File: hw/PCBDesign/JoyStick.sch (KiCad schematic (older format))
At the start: 4 parts

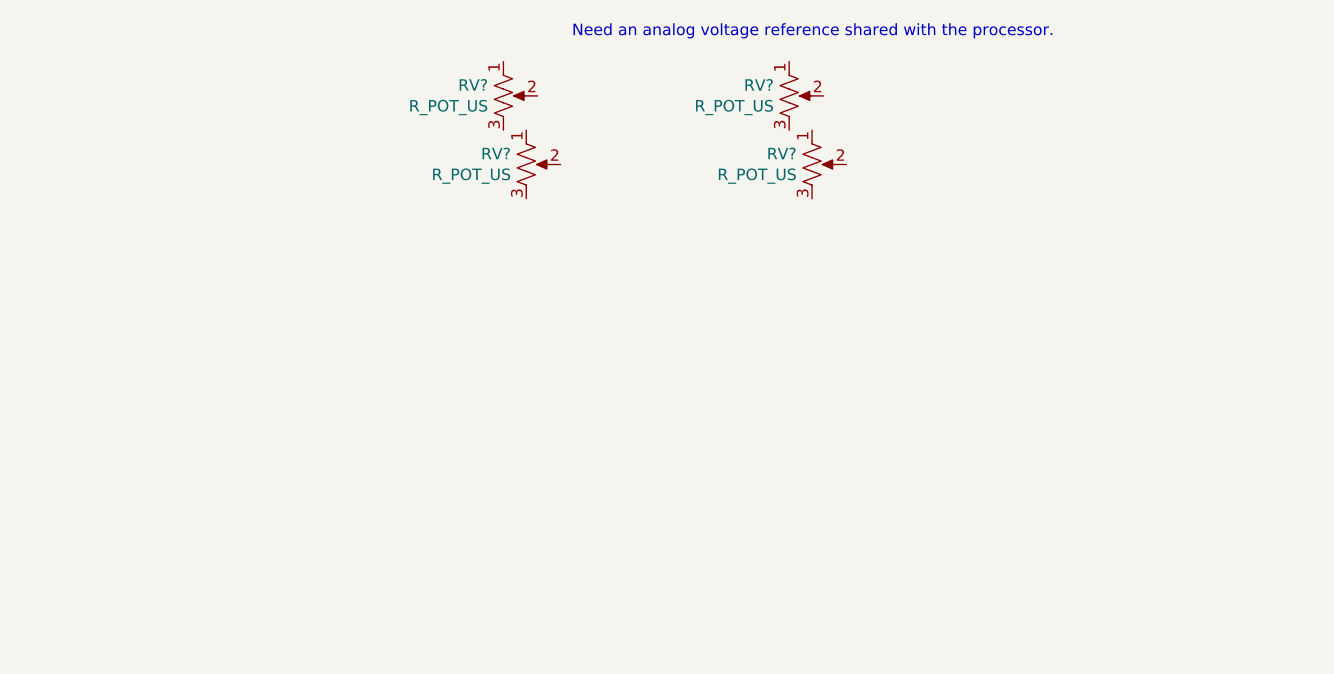
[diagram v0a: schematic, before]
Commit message: Add HMI input circuitry
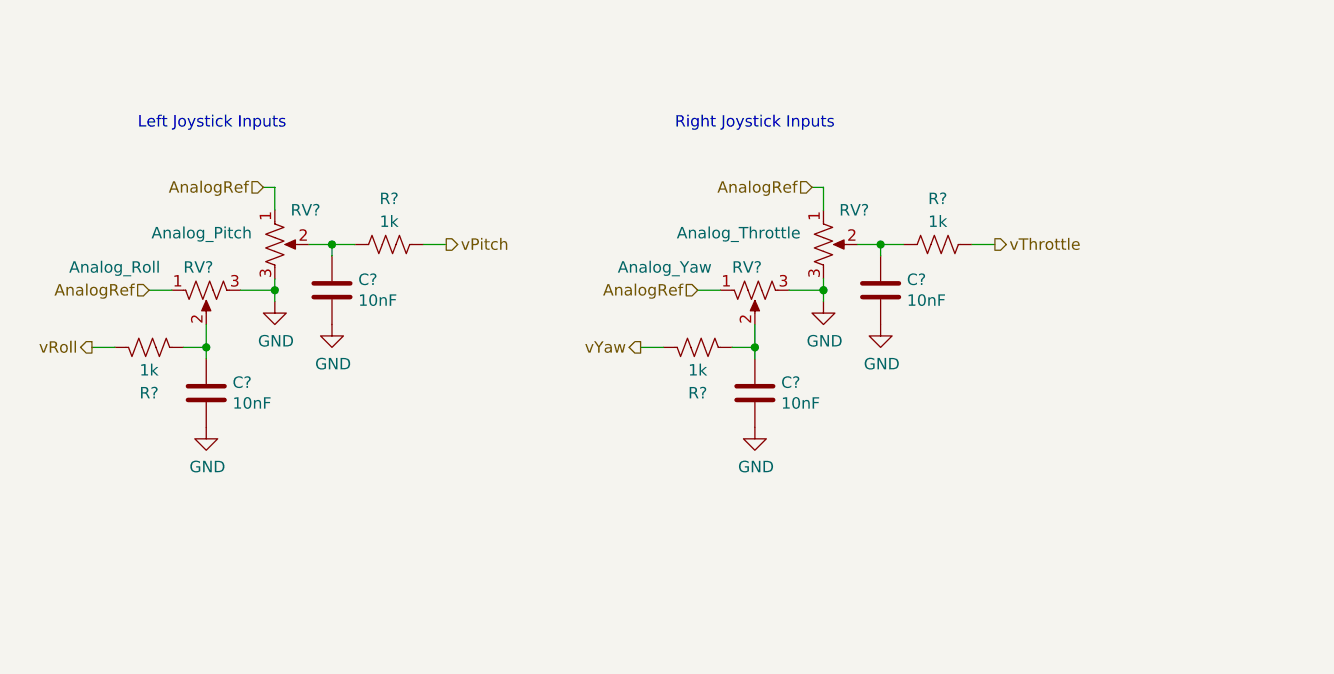
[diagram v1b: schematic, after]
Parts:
- removed RV? (x2): R_POT_US, symbol Device:R_POT_US
- added C? (x4): 10nF, symbol Device:C
- added R? (x4): 1k, symbol Device:R_US
- added RV?: Analog_Throttle, symbol Device:R_POT_US
- added RV?: Analog_Yaw, symbol Device:R_POT_US
- RV?: value R_POT_US -> Analog_Pitch
- RV?: value R_POT_US -> Analog_Roll
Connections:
- net AnalogRef: now reaches RV?.1
- net AnalogRef: now also RV?.1, RV?.1, RV?.1
- net at RV?.2: now also C?.1, R?.1
- net GND: now reaches RV?.3
- net GND: now also RV?.3, C?.2, C?.2, C?.2, C?.2, RV?.3, RV?.3
- net at RV?.2: now also C?.1, R?.2
- new net: C?.1, R?.1, RV?.2
- new net: C?.1, R?.2, RV?.2
- new net vPitch: R?.2
- new net vRoll: R?.1
- new net vThrottle: R?.2
- new net vYaw: R?.1
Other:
- note added: "Left Joystick Inputs"
- note added: "Right Joystick Inputs\n"
- note removed: "Need an analog voltage reference shared with the processor."
- moved on the sheet: RV?

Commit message: Schematic polishing
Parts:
- added J15: PR_Joystick, symbol Connector_Generic:Conn_01x04
- added J16: TY_Joystick, symbol Connector_Generic:Conn_01x04
- C22, C23, C24, C25: renamed from C?; value 10nF -> 10n; footprint (none) -> Capacitor_SMD:C_0402_1005Metric; LCSC (none) -> C15195
- R39, R40, R41, R42: renamed from R?; footprint (none) -> Resistor_SMD:R_0402_1005Metric; LCSC (none) -> C11702
- gave numbers to parts that had none: 4
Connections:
- net AnalogRef: now also J15.1 (Pin_1), J16.1 (Pin_1)
- net GND: now also J15.4 (Pin_4), J16.4 (Pin_4)
- net JS_2: now reaches C23.1, R40.1, RV2.2
- net JS_2: now also J15.2 (Pin_2)
- net JS_3: now reaches C22.1, R39.2, RV1.2
- net JS_3: now also J15.3 (Pin_3)
- net JS_0: now reaches C25.1, R42.1, RV4.2
- net JS_0: now also J16.2 (Pin_2)
- net JS_1: now reaches C24.1, R41.2, RV3.2
- net JS_1: now also J16.3 (Pin_3)
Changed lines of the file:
@@
 $EndDescr
 $Comp
-L Device:R_POT_US RV?
+L Device:R_POT_US RV2
 U 1 1 60453A22
 P 3350 3300
-F 0 "RV?" H 3550 3450 50  0000 R CNN
+F 0 "RV2" H 3550 3450 50  0000 R CNN
 F 1 "Analog_Pitch" H 3250 3350 50  0000 R CNN
 F 2 "" H 3350 3300 50  0001 C CNN
@@
 $EndComp
 $Comp
-L Device:R_POT_US RV?
+L Device:R_POT_US RV1
 U 1 1 60453A2E
 P 3050 3500
-F 0 "RV?" V 2950 3600 50  0000 R CNN
+F 0 "RV1" V 2950 3600 50  0000 R CNN
 F 1 "Analog_Roll" V 2950 4100 50  0000 R CNN
 F 2 "" H 3050 3500 50  0001 C CNN
@@
 $EndComp
 $Comp
-L power:GND #PWR?
+L power:GND #PWR050
 U 1 1 6047A14E
 P 3350 3550
-F 0 "#PWR?" H 3350 3300 50  0001 C CNN
+F 0 "#PWR050" H 3350 3300 50  0001 C CNN
 F 1 "GND" H 3355 3377 50  0000 C CNN
 F 2 "" H 3350 3550 50  0001 C CNN
@@
 	3350 3050 3350 3150
 $Comp
-L Device:C C?
+L Device:C C23
 U 1 1 6047AD32
 P 3600 3500
-F 0 "C?" H 3715 3546 50  0000 L CNN
-F 1 "10nF" H 3715 3455 50  0000 L CNN
-F 2 "" H 3638 3350 50  0001 C CNN
+F 0 "C23" H 3715 3546 50  0000 L CNN
+F 1 "10n" H 3715 3455 50  0000 L CNN
+F 2 "Capacitor_SMD:C_0402_1005Metric" H 3638 3350 50  0001 C CNN
 F 3 "~" H 3600 3500 50  0001 C CNN
+F 4 "C15195" H 3600 3500 50  0001 C CNN "LCSC"
 	1    3600 3500
 	1    0    0    -1
 $EndComp
 $Comp
-L power:GND #PWR?
+L power:GND #PWR051
 U 1 1 6047B9E2
 P 3600 3650
-F 0 "#PWR?" H 3600 3400 50  0001 C CNN
+F 0 "#PWR051" H 3600 3400 50  0001 C CNN
 F 1 "GND" H 3605 3477 50  0000 C CNN
 F 2 "" H 3600 3650 50  0001 C CNN
@@
 	3600 3300 3600 3350
 $Comp
-L Device:R_US R?
+L Device:R_US R40
 U 1 1 6047C069
 P 3850 3300
-F 0 "R?" V 4050 3300 50  0000 C CNN
+F 0 "R40" V 4050 3300 50  0000 C CNN
 F 1 "1k" V 3950 3300 50  0000 C CNN
-F 2 "" V 3890 3290 50  0001 C CNN
+F 2 "Resistor_SMD:R_0402_1005Metric" V 3890 3290 50  0001 C CNN
 F 3 "~" H 3850 3300 50  0001 C CNN
+F 4 "C11702" H 3850 3300 50  0001 C CNN "LCSC"
 	1    3850 3300
 	0    -1   -1   0
@@
 Connection ~ 3600 3300
 $Comp
-L Device:C C?
+L Device:C C22
 U 1 1 6047D084
 P 3050 3950
-F 0 "C?" H 3165 3996 50  0000 L CNN
-F 1 "10nF" H 3165 3905 50  0000 L CNN
-F 2 "" H 3088 3800 50  0001 C CNN
+F 0 "C22" H 3165 3996 50  0000 L CNN
+F 1 "10n" H 3165 3905 50  0000 L CNN
+F 2 "Capacitor_SMD:C_0402_1005Metric" H 3088 3800 50  0001 C CNN
 F 3 "~" H 3050 3950 50  0001 C CNN
+F 4 "C15195" H 3050 3950 50  0001 C CNN "LCSC"
 	1    3050 3950
 	1    0    0    -1
 $EndComp
 $Comp
-L Device:R_US R?
+L Device:R_US R39
 U 1 1 6047D627
 P 2800 3750
-F 0 "R?" V 3000 3750 50  0000 C CNN
+F 0 "R39" V 3000 3750 50  0000 C CNN
 F 1 "1k" V 2900 3750 50  0000 C CNN
-F 2 "" V 2840 3740 50  0001 C CNN
+F 2 "Resistor_SMD:R_0402_1005Metric" V 2840 3740 50  0001 C CNN
 F 3 "~" H 2800 3750 50  0001 C CNN
+F 4 "C11702" H 2800 3750 50  0001 C CNN "LCSC"
 	1    2800 3750
 	0    -1   1    0
 $EndComp
 $Comp
-L power:GND #PWR?
+L power:GND #PWR049
 U 1 1 6047E198
 P 3050 4100
-F 0 "#PWR?" H 3050 3850 50  0001 C CNN
+F 0 "#PWR049" H 3050 3850 50  0001 C CNN
 F 1 "GND" H 3055 3927 50  0000 C CNN
 F 2 "" H 3050 4100 50  0001 C CNN
@@
 	2550 3750 2650 3750
 $Comp
-L Device:R_POT_US RV?
+L Device:R_POT_US RV4
 U 1 1 60485882
 P 5750 3300
-F 0 "RV?" H 5950 3450 50  0000 R CNN
+F 0 "RV4" H 5950 3450 50  0000 R CNN
 F 1 "Analog_Throttle" H 5650 3350 50  0000 R CNN
 F 2 "" H 5750 3300 50  0001 C CNN
@@
 $EndComp
 $Comp
-L Device:R_POT_US RV?
+L Device:R_POT_US RV3
 U 1 1 60485888
 P 5450 3500
-F 0 "RV?" V 5350 3600 50  0000 R CNN
+F 0 "RV3" V 5350 3600 50  0000 R CNN
 F 1 "Analog_Yaw" V 5350 4100 50  0000 R CNN
 F 2 "" H 5450 3500 50  0001 C CNN
@@
 $EndComp
 $Comp
-L power:GND #PWR?
+L power:GND #PWR053
 U 1 1 6048588E
 P 5750 3550
-F 0 "#PWR?" H 5750 3300 50  0001 C CNN
+F 0 "#PWR053" H 5750 3300 50  0001 C CNN
 F 1 "GND" H 5755 3377 50  0000 C CNN
 F 2 "" H 5750 3550 50  0001 C CNN
@@
 	5750 3050 5750 3150
 $Comp
-L Device:C C?
+L Device:C C25
 U 1 1 6048589D
 P 6000 3500
-F 0 "C?" H 6115 3546 50  0000 L CNN
-F 1 "10nF" H 6115 3455 50  0000 L CNN
-F 2 "" H 6038 3350 50  0001 C CNN
+F 0 "C25" H 6115 3546 50  0000 L CNN
+F 1 "10n" H 6115 3455 50  0000 L CNN
+F 2 "Capacitor_SMD:C_0402_1005Metric" H 6038 3350 50  0001 C CNN
 F 3 "~" H 6000 3500 50  0001 C CNN
+F 4 "C15195" H 6000 3500 50  0001 C CNN "LCSC"
 	1    6000 3500
 	1    0    0    -1
 $EndComp
 $Comp
-L power:GND #PWR?
+L power:GND #PWR054
 U 1 1 604858A3
 P 6000 3650
-F 0 "#PWR?" H 6000 3400 50  0001 C CNN
+F 0 "#PWR054" H 6000 3400 50  0001 C CNN
 F 1 "GND" H 6005 3477 50  0000 C CNN
 F 2 "" H 6000 3650 50  0001 C CNN
@@
 	6000 3300 6000 3350
 $Comp
-L Device:R_US R?
+L Device:R_US R42
 U 1 1 604858AB
 P 6250 3300
-F 0 "R?" V 6450 3300 50  0000 C CNN
+F 0 "R42" V 6450 3300 50  0000 C CNN
 F 1 "1k" V 6350 3300 50  0000 C CNN
-F 2 "" V 6290 3290 50  0001 C CNN
+F 2 "Resistor_SMD:R_0402_1005Metric" V 6290 3290 50  0001 C CNN
 F 3 "~" H 6250 3300 50  0001 C CNN
+F 4 "C11702" H 6250 3300 50  0001 C CNN "LCSC"
 	1    6250 3300
 	0    -1   -1   0
@@
 Connection ~ 6000 3300
 $Comp
-L Device:C C?
+L Device:C C24
 U 1 1 604858B3
 P 5450 3950
-F 0 "C?" H 5565 3996 50  0000 L CNN
-F 1 "10nF" H 5565 3905 50  0000 L CNN
-F 2 "" H 5488 3800 50  0001 C CNN
+F 0 "C24" H 5565 3996 50  0000 L CNN
+F 1 "10n" H 5565 3905 50  0000 L CNN
+F 2 "Capacitor_SMD:C_0402_1005Metric" H 5488 3800 50  0001 C CNN
 F 3 "~" H 5450 3950 50  0001 C CNN
+F 4 "C15195" H 5450 3950 50  0001 C CNN "LCSC"
 	1    5450 3950
 	1    0    0    -1
 $EndComp
 $Comp
-L Device:R_US R?
+L Device:R_US R41
 U 1 1 604858B9
 P 5200 3750
-F 0 "R?" V 5400 3750 50  0000 C CNN
+F 0 "R41" V 5400 3750 50  0000 C CNN
 F 1 "1k" V 5300 3750 50  0000 C CNN
-F 2 "" V 5240 3740 50  0001 C CNN
+F 2 "Resistor_SMD:R_0402_1005Metric" V 5240 3740 50  0001 C CNN
 F 3 "~" H 5200 3750 50  0001 C CNN
+F 4 "C11702" H 5200 3750 50  0001 C CNN "LCSC"
 	1    5200 3750
 	0    -1   1    0
 $EndComp
 $Comp
-L power:GND #PWR?
+L power:GND #PWR052
 U 1 1 604858BF
 P 5450 4100
-F 0 "#PWR?" H 5450 3850 50  0001 C CNN
+F 0 "#PWR052" H 5450 3850 50  0001 C CNN
 F 1 "GND" H 5455 3927 50  0000 C CNN
 F 2 "" H 5450 4100 50  0001 C CNN
@@
 Text Notes 5100 2800 0    50   ~ 0
 Right Joystick Inputs\n
+$Comp
+L Connector_Generic:Conn_01x04 J16
+U 1 1 60531BA7
+P 7300 3550
+F 0 "J16" H 7380 3542 50  0000 L CNN
+F 1 "TY_Joystick" H 7380 3451 50  0000 L CNN
+F 2 "" H 7300 3550 50  0001 C CNN
+F 3 "~" H 7300 3550 50  0001 C CNN
+	1    7300 3550
+	1    0    0    -1
+$EndComp
+Wire Wire Line
+	7100 3650 6750 3650
+Wire Wire Line
+	6750 3550 7100 3550
+$Comp
+L power:GND #PWR0113
+U 1 1 60533290
+P 7100 3750
+F 0 "#PWR0113" H 7100 3500 50  0001 C CNN
+F 1 "GND" H 7105 3577 50  0000 C CNN
+F 2 "" H 7100 3750 50  0001 C CNN
+F 3 "" H 7100 3750 50  0001 C CNN
+	1    7100 3750
+	1    0    0    -1
+$EndComp
+Text HLabel 7100 3450 0    50   Input ~ 0
+AnalogRef
+Text Label 6750 3550 0    50   ~ 0
+JS_0
+Text Label 6750 3650 0    50   ~ 0
+JS_1
+Text Label 5400 3750 0    50   ~ 0
+JS_1
+Text Label 5950 3300 0    50   ~ 0
+JS_0
+$Comp
+L Connector_Generic:Conn_01x04 J15
+U 1 1 6053654A
+P 4100 4200
+F 0 "J15" H 4180 4192 50  0000 L CNN
+F 1 "PR_Joystick" H 4180 4101 50  0000 L CNN
+F 2 "" H 4100 4200 50  0001 C CNN
+F 3 "~" H 4100 4200 50  0001 C CNN
+	1    4100 4200
+	1    0    0    -1
+$EndComp
+Wire Wire Line
+	3900 4300 3550 4300
+Wire Wire Line
+	3550 4200 3900 4200
+$Comp
+L power:GND #PWR0112
+U 1 1 60536552
+P 3900 4400
+F 0 "#PWR0112" H 3900 4150 50  0001 C CNN
+F 1 "GND" H 3905 4227 50  0000 C CNN
+F 2 "" H 3900 4400 50  0001 C CNN
+F 3 "" H 3900 4400 50  0001 C CNN
+	1    3900 4400
+	1    0    0    -1
+$EndComp
+Text Label 3550 4200 0    50   ~ 0
+JS_2
+Text Label 3550 4300 0    50   ~ 0
+JS_3
+Text Label 3550 3300 0    50   ~ 0
+JS_2
+Text Label 3000 3750 0    50   ~ 0
+JS_3
+Text HLabel 3900 4100 0    50   Input ~ 0
+AnalogRef
 $EndSCHEMATC

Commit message: Added PCB
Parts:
- removed J15: PR_Joystick, symbol Connector_Generic:Conn_01x04
- removed J16: TY_Joystick, symbol Connector_Generic:Conn_01x04
- added J6: JoystickConn, Connector_JST:JST_PH_S8B-PH-SM4-TB_1x08-1MP_P2.00mm_Horizontal, symbol Connector_Generic:Conn_01x08
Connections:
- net AnalogRef: now also J6.1 (Pin_1), J6.5 (Pin_5)
- net GND: now also J6.4 (Pin_4), J6.8 (Pin_8)
- net JS_0: now also J6.2 (Pin_2)
- net JS_1: now also J6.3 (Pin_3)
- net JS_2: now also J6.6 (Pin_6)
- net JS_3: now also J6.7 (Pin_7)
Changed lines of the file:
@@
 Text Notes 5100 2800 0    50   ~ 0
 Right Joystick Inputs\n
-$Comp
-L Connector_Generic:Conn_01x04 J16
-U 1 1 60531BA7
-P 7300 3550
-F 0 "J16" H 7380 3542 50  0000 L CNN
-F 1 "TY_Joystick" H 7380 3451 50  0000 L CNN
-F 2 "" H 7300 3550 50  0001 C CNN
-F 3 "~" H 7300 3550 50  0001 C CNN
-	1    7300 3550
-	1    0    0    -1
-$EndComp
 Wire Wire Line
-	7100 3650 6750 3650
+	6900 4500 6550 4500
 Wire Wire Line
-	6750 3550 7100 3550
+	6550 4400 6900 4400
 $Comp
 L power:GND #PWR0113
 U 1 1 60533290
-P 7100 3750
-F 0 "#PWR0113" H 7100 3500 50  0001 C CNN
-F 1 "GND" H 7105 3577 50  0000 C CNN
-F 2 "" H 7100 3750 50  0001 C CNN
-F 3 "" H 7100 3750 50  0001 C CNN
-	1    7100 3750
-	1    0    0    -1
+P 6900 4600
+F 0 "#PWR0113" H 6900 4350 50  0001 C CNN
+F 1 "GND" H 6905 4427 50  0000 C CNN
+F 2 "" H 6900 4600 50  0001 C CNN
+F 3 "" H 6900 4600 50  0001 C CNN
+	1    6900 4600
+	0    1    1    0
 $EndComp
-Text HLabel 7100 3450 0    50   Input ~ 0
+Text HLabel 6900 4300 0    50   Input ~ 0
 AnalogRef
-Text Label 6750 3550 0    50   ~ 0
+Text Label 6550 4400 0    50   ~ 0
 JS_0
-Text Label 6750 3650 0    50   ~ 0
+Text Label 6550 4500 0    50   ~ 0
 JS_1
 Text Label 5400 3750 0    50   ~ 0
@@
 Text Label 5950 3300 0    50   ~ 0
 JS_0
-$Comp
-L Connector_Generic:Conn_01x04 J15
-U 1 1 6053654A
-P 4100 4200
-F 0 "J15" H 4180 4192 50  0000 L CNN
-F 1 "PR_Joystick" H 4180 4101 50  0000 L CNN
-F 2 "" H 4100 4200 50  0001 C CNN
-F 3 "~" H 4100 4200 50  0001 C CNN
-	1    4100 4200
-	1    0    0    -1
-$EndComp
 Wire Wire Line
-	3900 4300 3550 4300
+	6900 4900 6550 4900
 Wire Wire Line
-	3550 4200 3900 4200
+	6550 4800 6900 4800
 $Comp
 L power:GND #PWR0112
 U 1 1 60536552
-P 3900 4400
-F 0 "#PWR0112" H 3900 4150 50  0001 C CNN
-F 1 "GND" H 3905 4227 50  0000 C CNN
-F 2 "" H 3900 4400 50  0001 C CNN
-F 3 "" H 3900 4400 50  0001 C CNN
-	1    3900 4400
-	1    0    0    -1
+P 6900 5000
+F 0 "#PWR0112" H 6900 4750 50  0001 C CNN
+F 1 "GND" H 6905 4827 50  0000 C CNN
+F 2 "" H 6900 5000 50  0001 C CNN
+F 3 "" H 6900 5000 50  0001 C CNN
+	1    6900 5000
+	0    1    1    0
 $EndComp
-Text Label 3550 4200 0    50   ~ 0
+Text Label 6550 4800 0    50   ~ 0
 JS_2
-Text Label 3550 4300 0    50   ~ 0
+Text Label 6550 4900 0    50   ~ 0
 JS_3
 Text Label 3550 3300 0    50   ~ 0
@@
 Text Label 3000 3750 0    50   ~ 0
 JS_3
-Text HLabel 3900 4100 0    50   Input ~ 0
+Text HLabel 6900 4700 0    50   Input ~ 0
 AnalogRef
+$Comp
+L Connector_Generic:Conn_01x08 J6
+U 1 1 605026C0
+P 7100 4600
+F 0 "J6" H 7180 4592 50  0000 L CNN
+F 1 "JoystickConn" H 7180 4501 50  0000 L CNN
+F 2 "Connector_JST:JST_PH_S8B-PH-SM4-TB_1x08-1MP_P2.00mm_Horizontal" H 7100 4600 50  0001 C CNN
+F 3 "~" H 7100 4600 50  0001 C CNN
+F 4 "455-1755-2-ND" H 7100 4600 50  0001 C CNN "DigiKey"
+	1    7100 4600
+	1    0    0    -1
+$EndComp
 $EndSCHEMATC

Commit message: HW updates. Testing out SPIFFS
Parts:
- J6: footprint Connector_JST:JST_PH_S8B-PH-SM4-TB_1x08-1MP_P2.00mm_Horizontal -> Connector_JST:JST_PH_B8B-PH-SM4-TB_1x08-1MP_P2.00mm_Vertical; DigiKey 455-1755-2-ND -> 455-1740-2-ND
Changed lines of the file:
@@
 F 0 "J6" H 7180 4592 50  0000 L CNN
 F 1 "JoystickConn" H 7180 4501 50  0000 L CNN
-F 2 "Connector_JST:JST_PH_S8B-PH-SM4-TB_1x08-1MP_P2.00mm_Horizontal" H 7100 4600 50  0001 C CNN
+F 2 "Connector_JST:JST_PH_B8B-PH-SM4-TB_1x08-1MP_P2.00mm_Vertical" H 7100 4600 50  0001 C CNN
 F 3 "~" H 7100 4600 50  0001 C CNN
-F 4 "455-1755-2-ND" H 7100 4600 50  0001 C CNN "DigiKey"
+F 4 "455-1740-2-ND" H 7100 4600 50  0001 C CNN "DigiKey"
 	1    7100 4600
 	1    0    0    -1

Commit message: Start working on PCB rev 2.0
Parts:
- J6: footprint Connector_JST:JST_PH_B8B-PH-SM4-TB_1x08-1MP_P2.00mm_Vertical -> Connector_Molex:Molex_PicoBlade_53261-0871_1x08-1MP_P1.25mm_Horizontal; DigiKey 455-1740-2-ND -> WM26501CT-ND
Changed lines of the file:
@@
 F 0 "J6" H 7180 4592 50  0000 L CNN
 F 1 "JoystickConn" H 7180 4501 50  0000 L CNN
-F 2 "Connector_JST:JST_PH_B8B-PH-SM4-TB_1x08-1MP_P2.00mm_Vertical" H 7100 4600 50  0001 C CNN
+F 2 "Connector_Molex:Molex_PicoBlade_53261-0871_1x08-1MP_P1.25mm_Horizontal" H 7100 4600 50  0001 C CNN
 F 3 "~" H 7100 4600 50  0001 C CNN
-F 4 "455-1740-2-ND" H 7100 4600 50  0001 C CNN "DigiKey"
+F 4 "WM26501CT-ND" H 7100 4600 50  0001 C CNN "DigiKey"
 	1    7100 4600
 	1    0    0    -1
